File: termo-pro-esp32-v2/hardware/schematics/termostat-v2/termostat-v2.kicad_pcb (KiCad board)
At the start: 2 copper layers, 0 parts

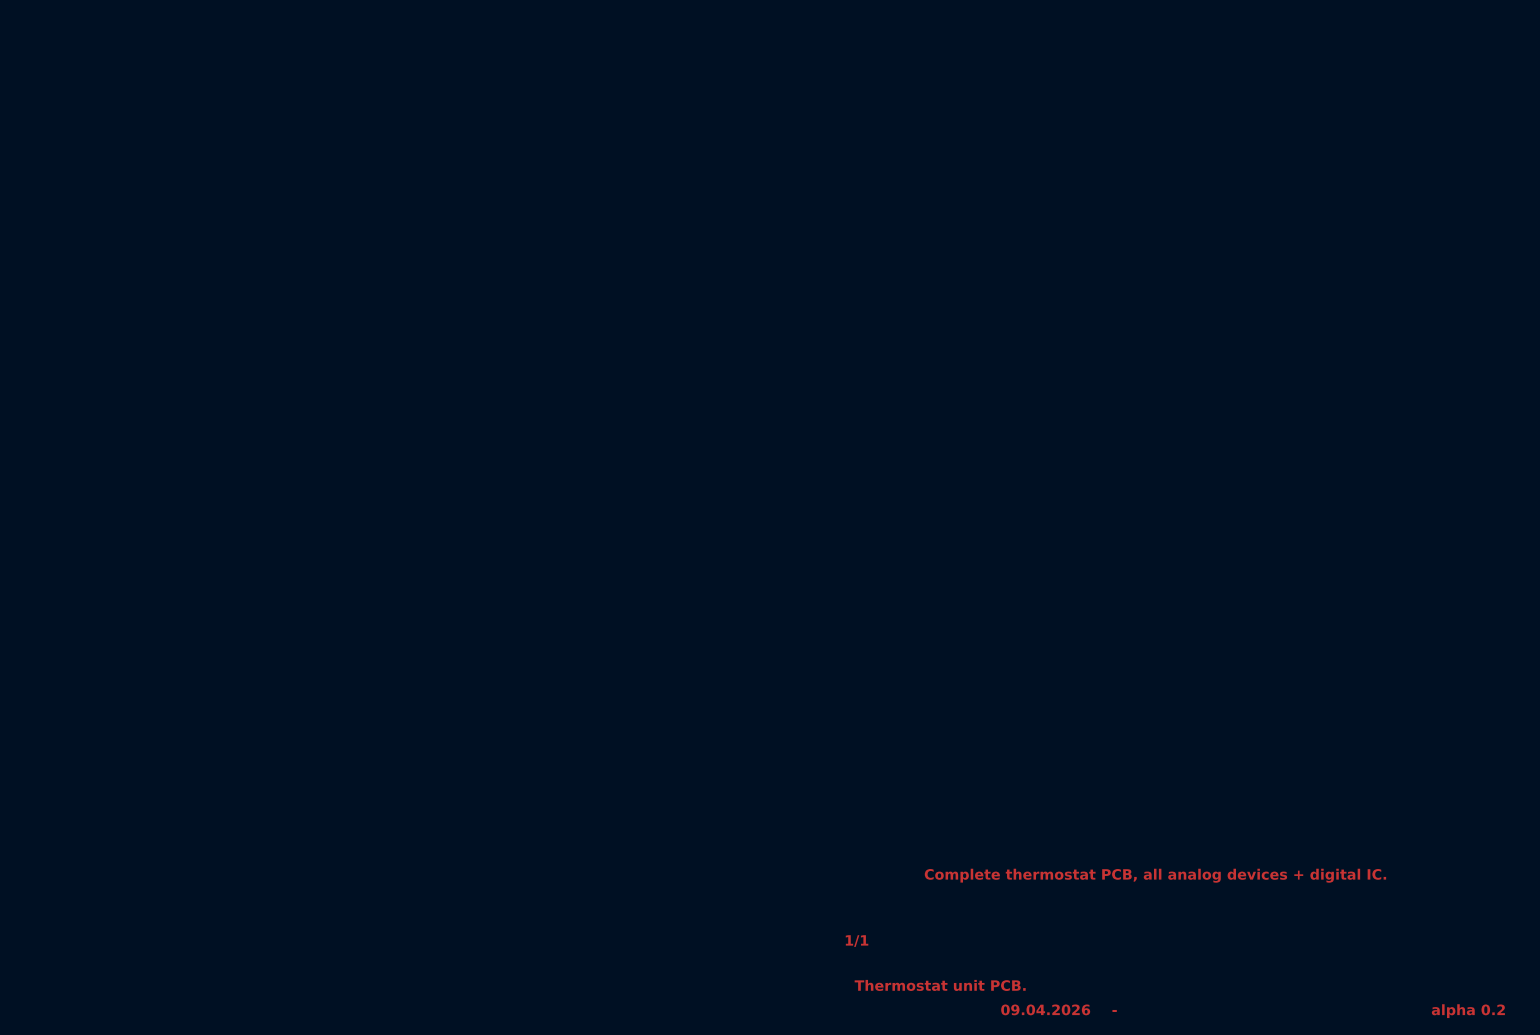
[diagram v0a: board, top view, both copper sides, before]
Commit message: Starting Unit PCB compleate.
Some footprint issues were encountered on the initial unit PCB, regarding the ceramic capacitors and the 1×02 5.08 mm screw terminal.

-In the thermostat schematic, the ceramic capacitors were updated to a disc footprint , as well in the starting unit scheme.

-Thermostat PCB is currently in progress.
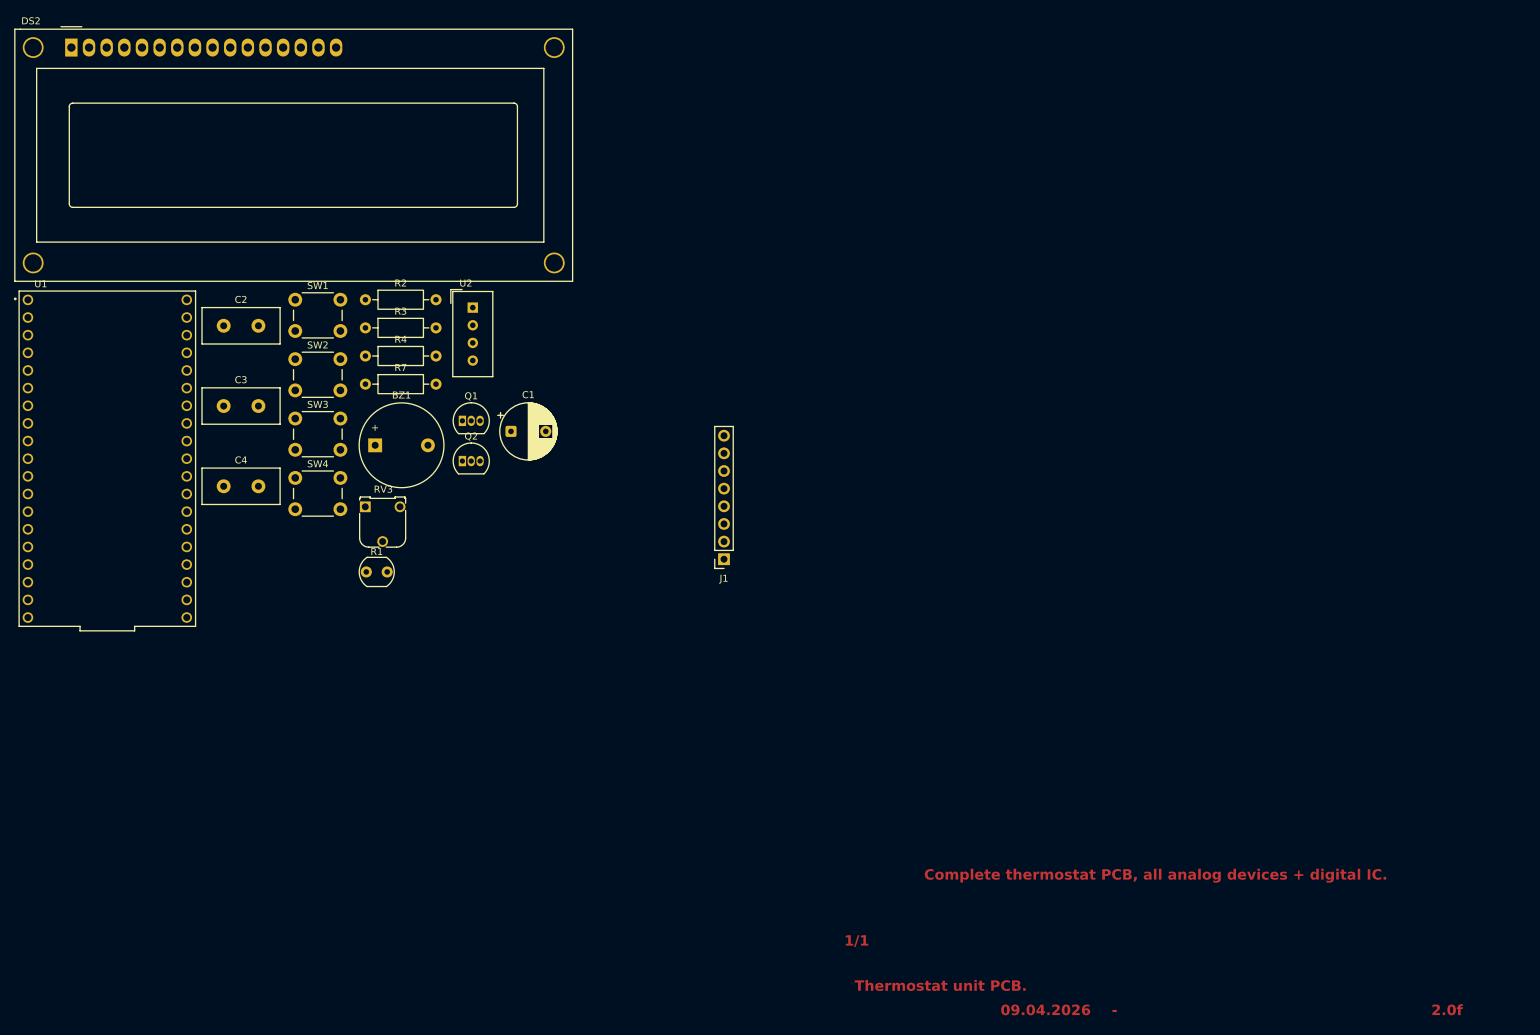
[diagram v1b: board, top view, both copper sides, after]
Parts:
- added BZ1: Buzzer, Buzzer_Beeper:Buzzer_12x9.5RM7.6, F.Cu at (119.0, 111.8)
- added C1: 25V 220uF, Capacitor_THT:CP_Radial_D8.0mm_P5.00mm, F.Cu at (138.5, 109.8)
- added C2: 50V 220nF, Capacitor_THT:C_Disc_D11.0mm_W5.0mm_P5.00mm, F.Cu at (97.2, 94.6)
- added C3: 50V 220nF, Capacitor_THT:C_Disc_D11.0mm_W5.0mm_P5.00mm, F.Cu at (97.2, 106.2)
- added C4: 50V 220nF, Capacitor_THT:C_Disc_D11.0mm_W5.0mm_P5.00mm, F.Cu at (97.2, 117.7)
- added DS2: WC1602A, Display:WC1602A, F.Cu at (75.3, 54.6)
- added J1: Conn_01x08_Pin, Connector_PinSocket_2.54mm:PinSocket_1x08_P2.54mm_Vertical, F.Cu at (169.2, 128.2)
- added Q1: PN2222A, Package_TO_SOT_THT:TO-92_Inline, F.Cu at (131.6, 108.3)
- added Q2: PN2222A, Package_TO_SOT_THT:TO-92_Inline, F.Cu at (131.6, 114.1)
- added R1: 10k, OptoDevice:R_LDR_5.0x4.1mm_P3mm_Vertical, F.Cu at (117.7, 130.0)
- added R2: 10k, Resistor_THT:R_Axial_DIN0207_L6.3mm_D2.5mm_P10.16mm_Horizontal, F.Cu at (117.6, 90.9)
- added R3: 10k, Resistor_THT:R_Axial_DIN0207_L6.3mm_D2.5mm_P10.16mm_Horizontal, F.Cu at (117.6, 94.9)
- added R4: 1k, Resistor_THT:R_Axial_DIN0207_L6.3mm_D2.5mm_P10.16mm_Horizontal, F.Cu at (117.6, 99.0)
- added R7: 330, Resistor_THT:R_Axial_DIN0207_L6.3mm_D2.5mm_P10.16mm_Horizontal, F.Cu at (117.6, 103.0)
- added RV3: 10k, Potentiometer_THT:Potentiometer_Runtron_RM-065_Vertical, F.Cu at (117.6, 120.7)
- added SW1: SW_Push, Button_Switch_THT:SW_PUSH_6mm, F.Cu at (107.5, 90.9)
- added SW2: SW_Push, Button_Switch_THT:SW_PUSH_6mm, F.Cu at (107.5, 99.4)
- added SW3: SW_Push, Button_Switch_THT:SW_PUSH_6mm, F.Cu at (107.5, 108.0)
- added SW4: SW_Push, Button_Switch_THT:SW_PUSH_6mm, F.Cu at (107.5, 116.5)
- added U1: NODEMCU-32S, NODEMCU-ESP32S:MODULE_NODEMCU-32S, F.Cu at (80.5, 113.7)
- added U2: DHT11, Sensor:Aosong_DHT11_5.5x12.0_P2.54mm, F.Cu at (133.1, 92.0)
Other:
- board text added: "2.0f"
- board text removed: "alpha 0.2"
